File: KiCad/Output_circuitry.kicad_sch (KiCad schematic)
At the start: 13 parts, among them IC1 TPS63070RNMR, IC2 ISL23511WFB8Z

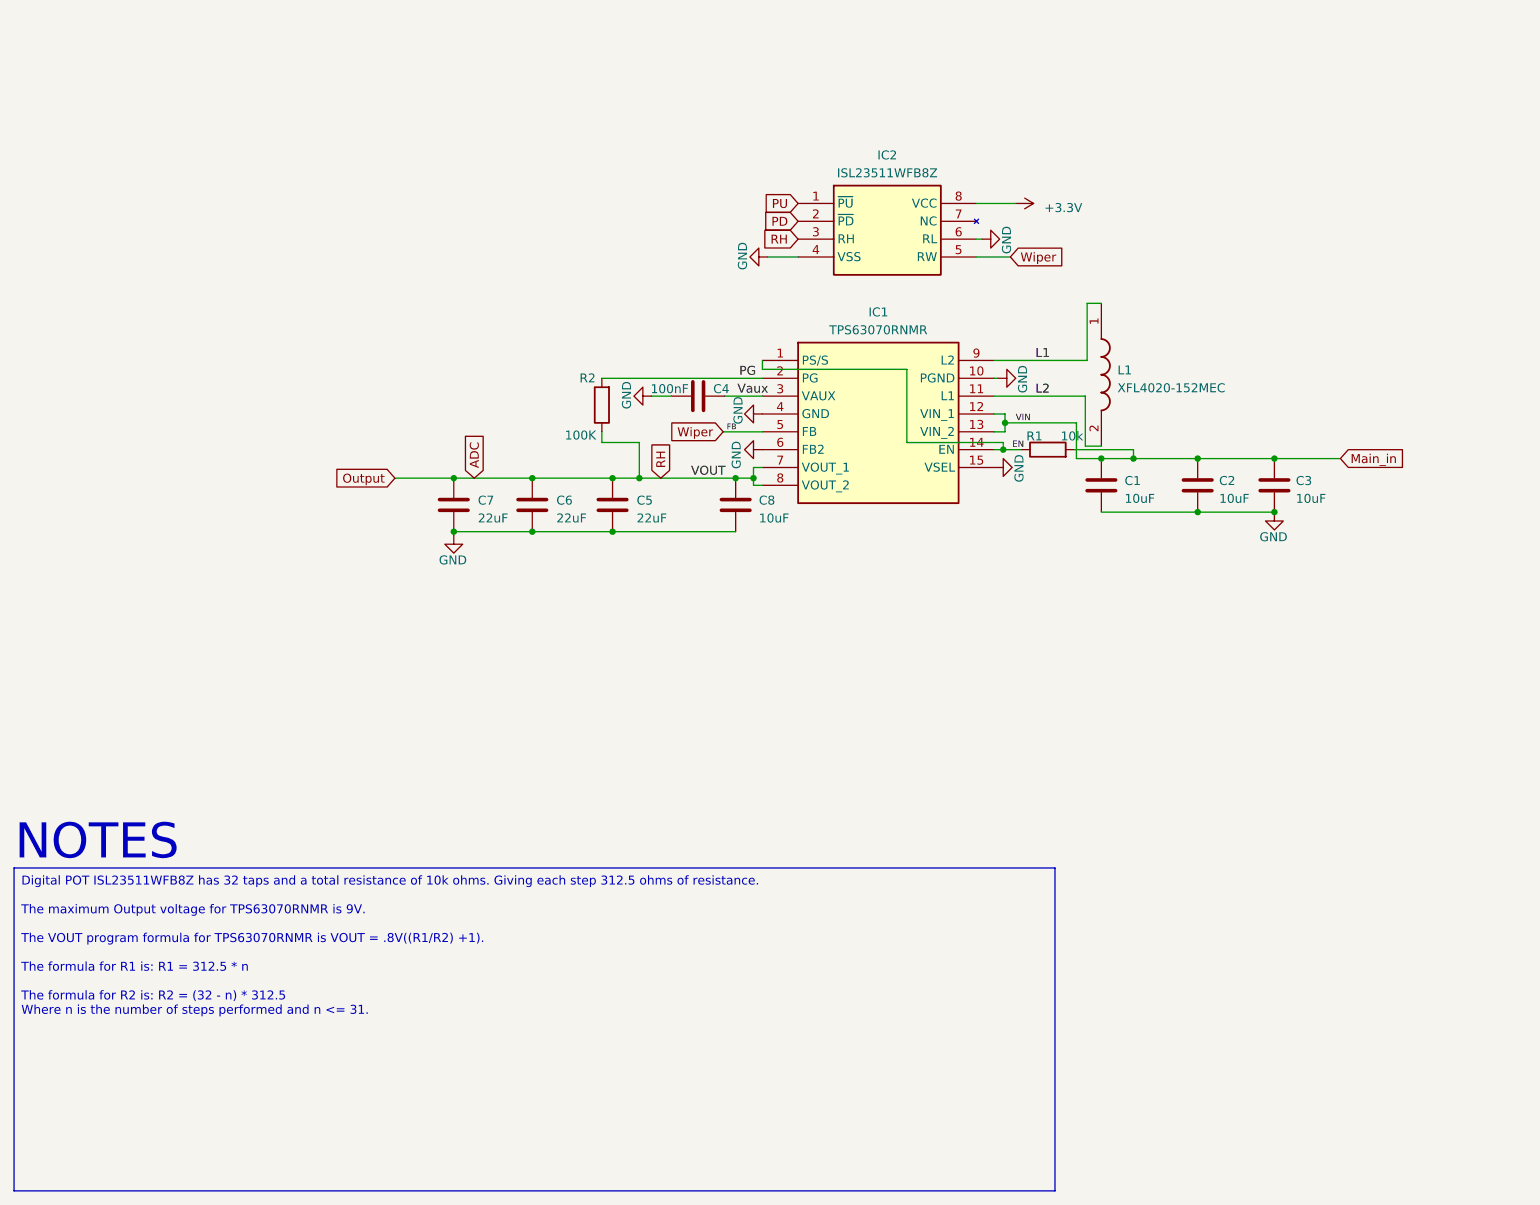
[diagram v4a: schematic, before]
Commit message: pushing ofr system reset
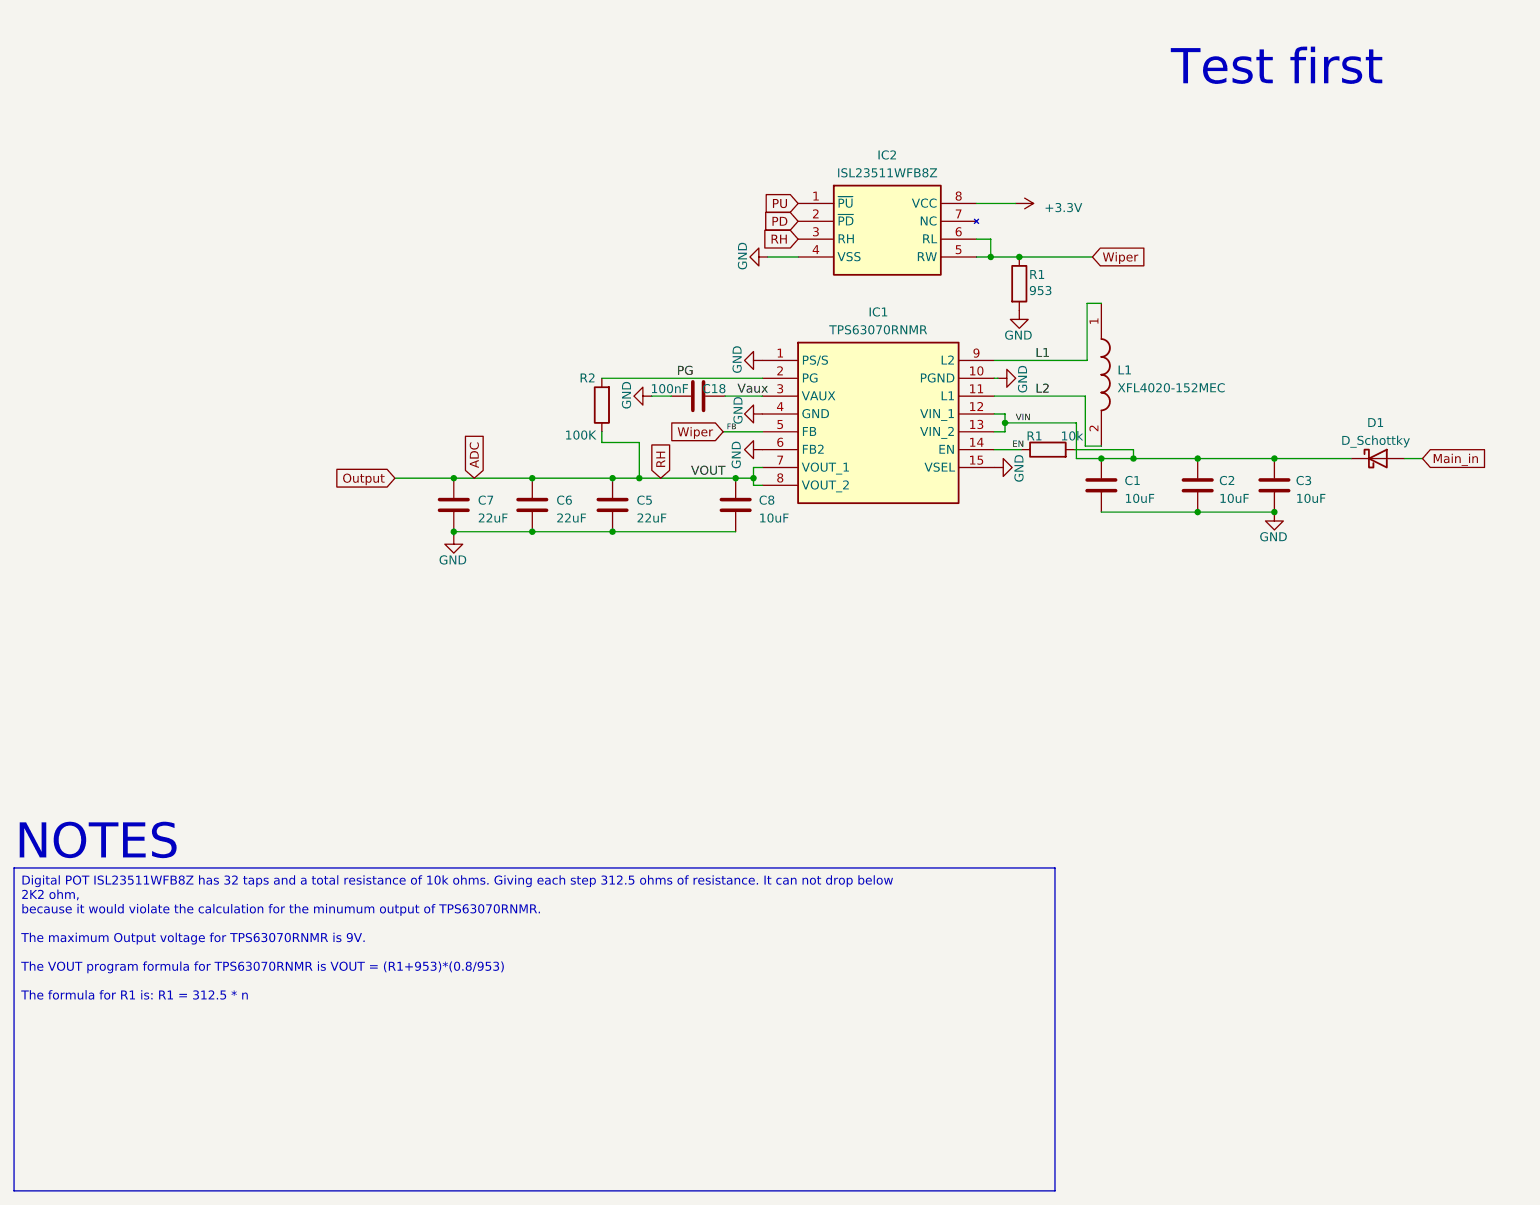
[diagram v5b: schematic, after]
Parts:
- removed C4: 100nF, Capacitor_SMD:C_0402_1005Metric_Pad0.74x0.62mm_HandSolder, symbol Device:C
- added C18: 100nF, Capacitor_SMD:C_0805_2012Metric_Pad1.18x1.45mm_HandSolder, symbol Device:C
- added D1: D_Schottky, Diode_SMD:D_MicroSMP_AK, symbol Device:D_Schottky
- added R1: 953, Resistor_SMD:R_0805_2012Metric_Pad1.20x1.40mm_HandSolder, symbol Device:R
- R1: footprint Resistor_SMD:R_0402_1005Metric_Pad0.72x0.64mm_HandSolder -> Resistor_SMD:R_0805_2012Metric_Pad1.20x1.40mm_HandSolder
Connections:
- net EN: no longer IC1.1 (PS/S)
- net GND: now also IC1.1 (PS/S), C18.1, R1.2; no longer IC2.6 (RL)
- net Main_in: now also D1.2 (A); no longer C1.1, C2.1, C3.1, IC1.12 (VIN_1), IC1.13 (VIN_2), R1.2
- net Vaux: now also C18.2
- net Wiper: now also IC2.6 (RL), R1.1
- new net VIN: C1.1, C2.1, C3.1, D1.1 (K), IC1.12 (VIN_1), IC1.13 (VIN_2), R1.2
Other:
- note added: "Test first"

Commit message: Replaced pot.
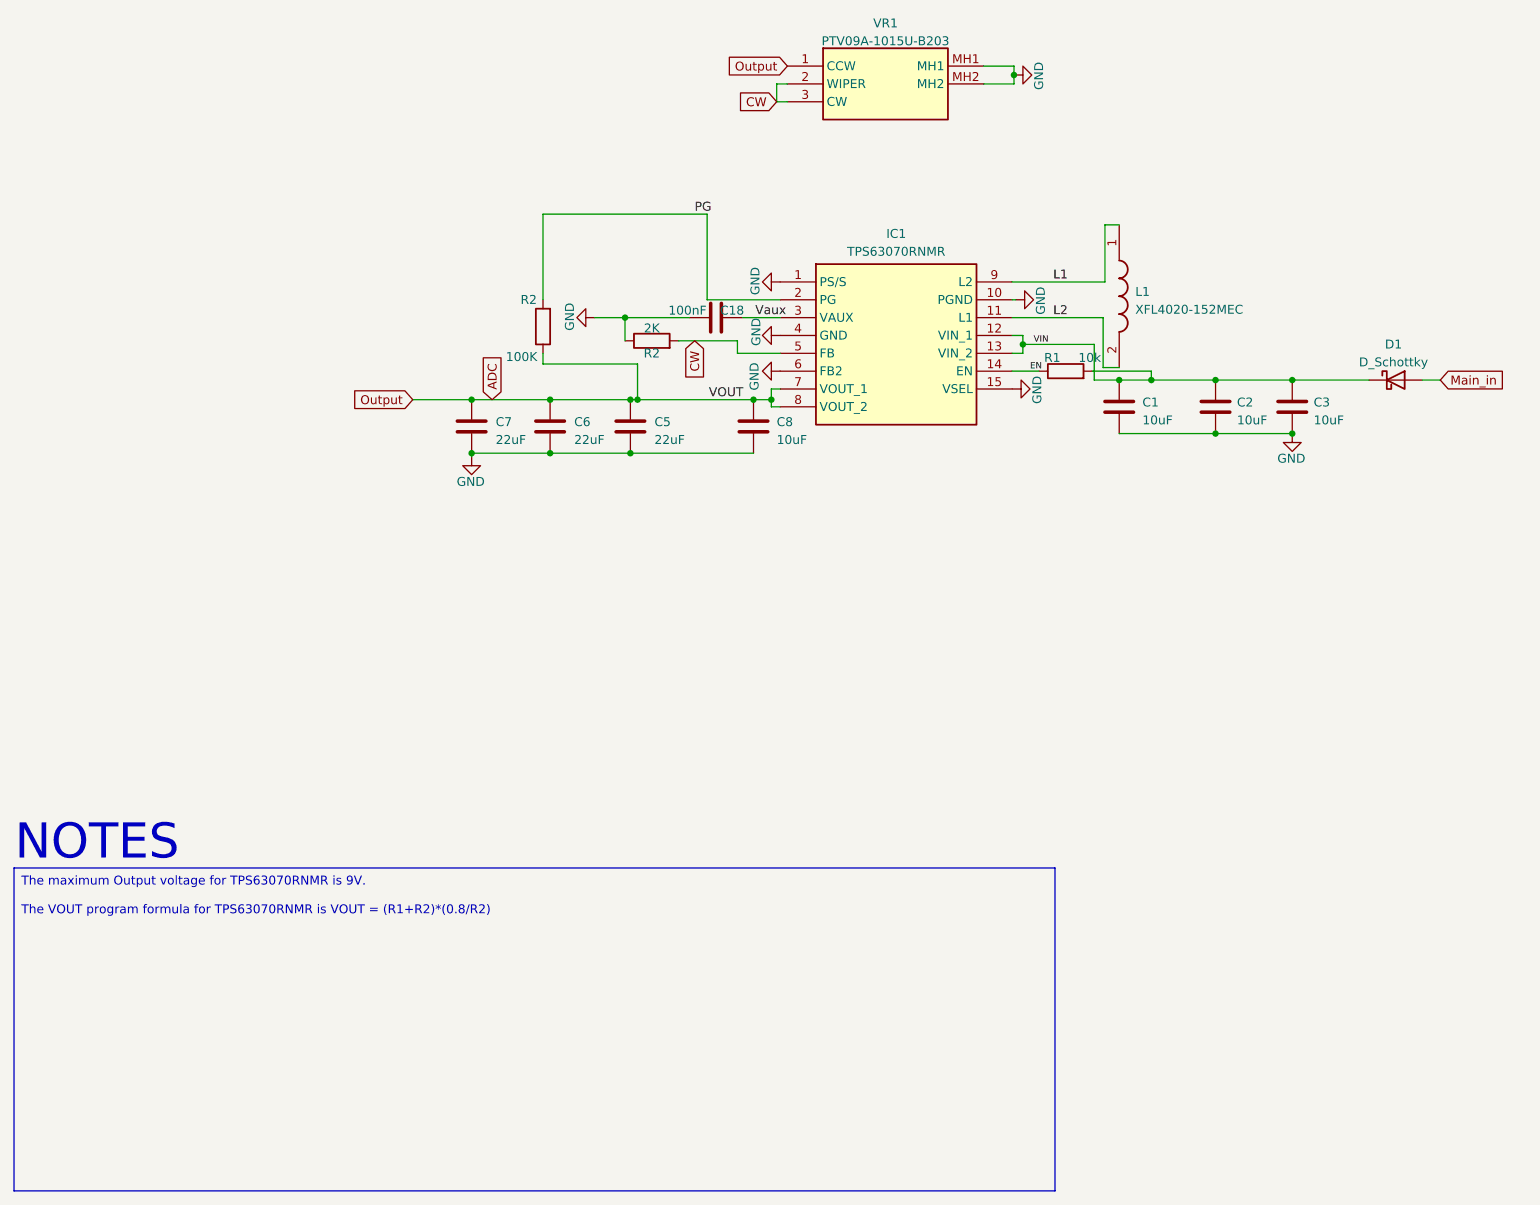
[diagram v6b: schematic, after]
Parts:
- removed IC2: ISL23511WFB8Z, Custom_eric:ISL23511WFB8Z, symbol Custom_eric:ISL23511WFB8Z
- removed R1: 953, Resistor_SMD:R_0805_2012Metric_Pad1.20x1.40mm_HandSolder, symbol Device:R
- added R2: 2K, Resistor_SMD:R_0805_2012Metric_Pad1.20x1.40mm_HandSolder, symbol Device:R
- added VR1: PTV09A-1015U-B203, SamacSys_Parts:PTV09A1015UB203, symbol SamacSys_Parts:PTV09A-1015U-B203
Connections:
- net ADC: now also VR1.1 (CCW)
- net GND: now also R2.1, VR1.MH1, VR1.MH2
- net Wiper renamed CW
- net CW: now also R2.2, VR1.2 (WIPER), VR1.3 (CW)
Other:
- note removed: "Test first"
- moved on the sheet: C1, C18, C2, C3, C5, C6, C7, C8, D1, IC1, L1, R1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
